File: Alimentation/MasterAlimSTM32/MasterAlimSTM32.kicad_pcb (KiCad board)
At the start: 2 copper layers, 67 parts, among them J1 Ext-Con, J10 Interf-Reg1, J11 AU Logic, J12 Interf-Reg2, J13 Interf-Reg3, J14 Interf-Reg4, J2 5V, J3 Bat. IN, J5 Direct Out, J6 Reg 1, J7 Reg 2, J8 Reg 3, J9 Reg 4, Q1 BSS138, Q2 BSS138, Q3 BSS138, Q4 BSS138, Q5 BSS138, Q6 BSS138, U1 PTN78060W_EUW-7, U2 STM32F405RGTx, U3 ACS712xLCTR-20A, U4 PTN78060W_EUW-7, U7 ACS712xLCTR-20A

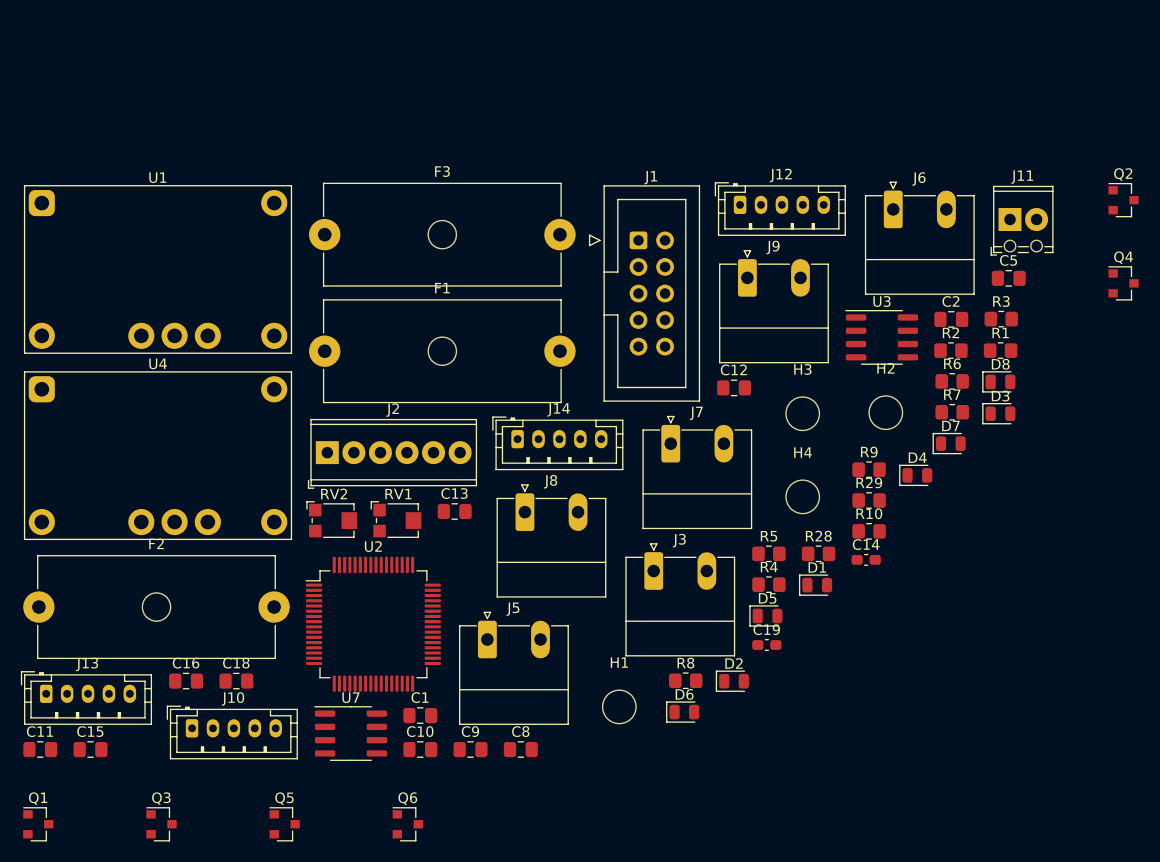
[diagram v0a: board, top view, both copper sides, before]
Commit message: Module alim ISO, clean master alim
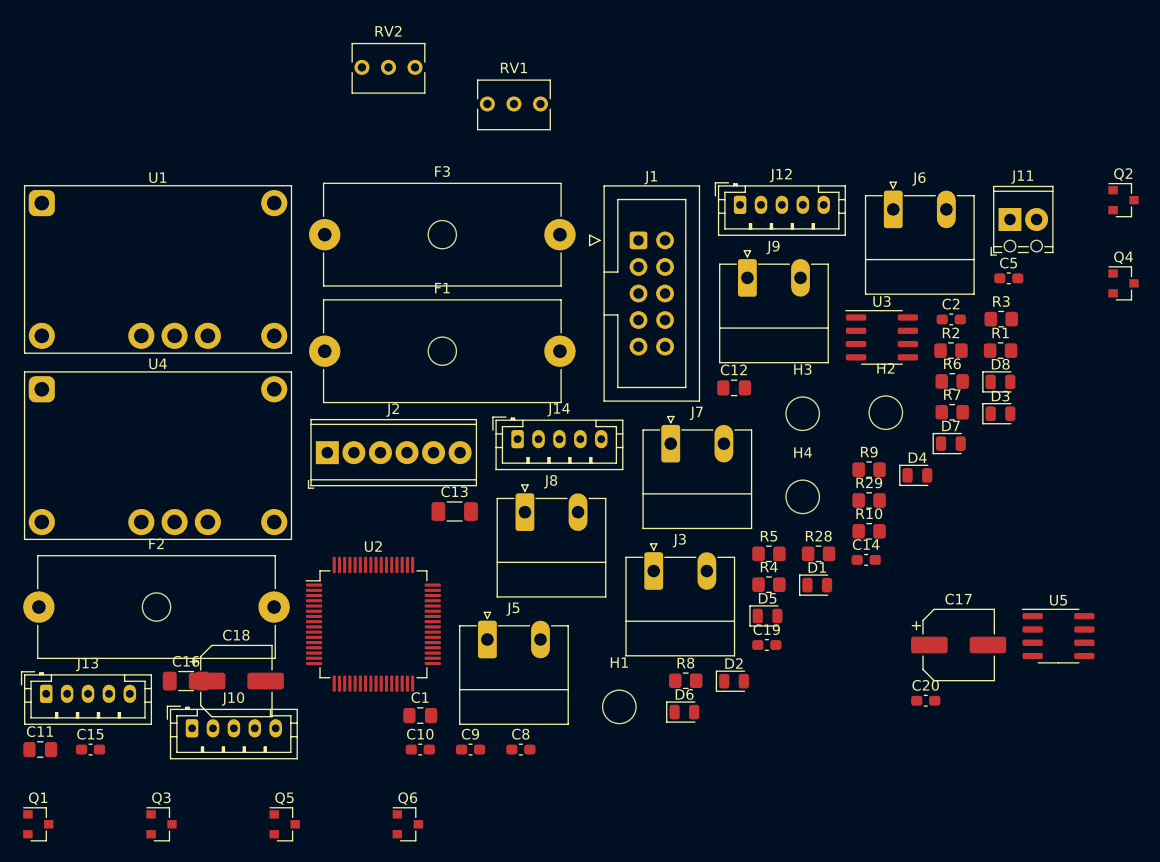
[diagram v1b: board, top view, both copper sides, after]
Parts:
- removed U7: ACS712xLCTR-20A, Package_SO:SOIC-8_3.9x4.9mm_P1.27mm
- added C17: 100u, Capacitor_SMD:CP_Elec_6.3x5.4, F.Cu at (183.5, 112.2)
- added C20: 100n, Capacitor_SMD:C_0603_1608Metric_Pad1.08x0.95mm_HandSolder, F.Cu at (180.3, 117.6)
- added U5: ACS712xLCTR-20A, Package_SO:SOIC-8_3.9x4.9mm_P1.27mm, F.Cu at (193.1, 111.4)
- C10, C15, C2, C5, C8, C9: footprint Capacitor_SMD:C_0805_2012Metric_Pad1.18x1.45mm_HandSolder -> Capacitor_SMD:C_0603_1608Metric_Pad1.08x0.95mm_HandSolder
- C13, C16: footprint Capacitor_SMD:C_0805_2012Metric_Pad1.18x1.45mm_HandSolder -> Capacitor_SMD:C_1206_3216Metric_Pad1.33x1.80mm_HandSolder
- C18: value 100n -> 100u; footprint Capacitor_SMD:C_0805_2012Metric_Pad1.18x1.45mm_HandSolder -> Capacitor_SMD:CP_Elec_6.3x5.4
- RV1, RV2: footprint Potentiometer_SMD:Potentiometer_Bourns_TC33X_Vertical -> Potentiometer_THT:Potentiometer_Bourns_3266Y_Vertical
- U1, U4: footprint Module:Texas_EUW_R-PDSS-T7_THT -> ARIG:Texas_EUW_R-PDSS-T7_THT
- moved RV2 44.0 mm to (131.5, 57.0)
- moved RV1 42.1 mm to (143.5, 60.5)
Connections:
- C10 pad 1: +3V3 -> GND
- C10 pad 2: GND -> +3V3
- C18 pad 1: GND -> Net-(C18-Pad1)
- C18 pad 2: +5V -> GND
- C2 pad 1: +3V3 -> GND
- C2 pad 2: GND -> +3V3
- C5 pad 1: +3V3 -> GND
- C5 pad 2: GND -> +3V3
- C8 pad 1: +3V3 -> GND
- C8 pad 2: GND -> +3V3
- C9 pad 1: +3V3 -> GND
- C9 pad 2: GND -> +3V3
- F3 pad 1: Net-(C20-Pad1) -> Net-(C18-Pad1)
- U4 pad 5: Net-(C20-Pad1) -> Net-(C18-Pad1)
- U4 pad 6: Net-(C20-Pad1) -> Net-(C18-Pad1)
